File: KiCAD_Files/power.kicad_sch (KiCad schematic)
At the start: 100 parts, among them J1 Conn_01x01, J2 Conn_01x01, J3 Conn_01x01, J5 Conn_01x01, J8 Conn_01x01, K1 HF140FF/012-2HSWTF, Q11 NMOS, T1 Transformer_1P_1S, T2 Transformer_1P_1S, U1 INA240A1PW, U2 INA240A1PWR, U3 UCC27282DRC, U4 UCC27282DRC

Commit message: First routing pass complete.
Signed-off-by: Jean Alinei <jean.alinei@owntech.org>
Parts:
- removed C2, C4: C_Small, Capacitor_SMD:C_0805_2012Metric, symbol Device:C_Small
- removed C55: C, symbol Device:C
- added C101, C102: 4.7uF, Capacitor_SMD:C_0805_2012Metric, symbol Device:C_Small
- added C103, C110: 10µF, Capacitor_SMD:C_1206_3216Metric, symbol Device:C
- added C104, C105, C106, C107, C108, C109: C, Capacitor_SMD:C_1206_3216Metric, symbol Device:C
- added C111: 47uF, Capacitor_SMD:C_Elec_10x10.2, symbol Device:C_Polarized
- added C112: 47uH, Capacitor_SMD:C_Elec_10x10.2, symbol Device:C_Polarized
- added C113: ?nF, Capacitor_THT:C_Rect_L16.5mm_W7.0mm_P15.00mm_MKT, symbol Device:C_Small
- added C114, C115: 1nF, Capacitor_SMD:C_1210_3225Metric, symbol Device:C
- added D101, D102: D, Footprints:D_SOD-123, symbol Device:D
- added F101: 2.5A, Footprints:FUSE-TH_L8.4-W4.1-P5.08-D0.6, symbol Device:Fuse
- added HS101, HS102, HS103, HS104, HS105, HS106, HS107, HS108, HS109, HS11, HS12, HS5: 5x3mm pad 3mm high, Footprints:BTC-533-ZN01, symbol Mechanical:Heatsink_Pad
- added Logo101: ~, Footprints:owntech_mini10, symbol Symbols:Logo
- added R102, R103: 3.3R, Resistor_SMD:R_0805_2012Metric, symbol Device:R_Small
- added R104, R105, R106, R107, R108: 20, Resistor_SMD:R_0603_1608Metric, symbol Device:R_Small
- added R109: 20k, Resistor_SMD:R_0603_1608Metric, symbol Device:R_Small
- added RV101, RV102, RV103: TMOV14RP275, Varistor:RV_Disc_D12mm_W6.2mm_P7.5mm, symbol Device:Varistor
- C22, C27, C33, C38: footprint Capacitor_THT:C_Rect_L16.5mm_W8.7mm_P15.00mm_MKT -> Footprints:C_Rect_L16.5mm_W8mm_P15.00mm_MKT
- C39: footprint (none) -> Capacitor_SMD:C_0805_2012Metric
- D5: value D_Schottky -> 40V - BAT165E6327F; footprint Diode_SMD:D_SMA -> Diode_SMD:D_SOD-323; LCSC (none) -> C42411276
- F1: value T5A250V -> 2.5A; LCSC C42367993 -> C2995772
- FL1, FL2: symbol Device:Filter_EMI_CommonMode -> Device:L_Coupled_1243
- FL3: value ~ -> 1mH; footprint (none) -> Footprints:IND-TH_4P-L23.0-W15.0-P7.50-D1.0-S9.0; symbol Device:Filter_EMI_CommonMode -> Device:L_Coupled_1243
- Q1, Q2, Q3, Q4: value ~ -> CID12N65D
- Q10, Q5, Q6, Q7, Q8, Q9: value ~ -> CJAC90SN12
- Q11: value NMOS -> ZXMN7A11GTA; symbol Simulation_SPICE:NMOS -> Transistor_FET:Q_NMOS_GDSD; LCSC (none) -> C460277
- R101, R32, R33, R6, R8, R9: footprint Resistor_SMD:R_0805_2012Metric -> Resistor_SMD:R_0603_1608Metric
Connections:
- net Earth is gone; now on net Earth_Protective: J3.1 (Pin_1)
- net +12V_{HV}: now also D101.2 (A), D102.2 (A)
- net +12V_{SN1}: now also C101.1, R102.1
- net +12V_{SN2}: now also C102.1, R103.1
- net AC Current sense/In+: now also F101.1; no longer J2.1 (Pin_1)
- net AC Current sense/In-: now also FL2.3; no longer FL2.4
- net Earth_Protective: now also RV102.2, RV103.2
- net GND_{HV}: now also C114.2, C115.2, HS102.1, HS103.1
- net GND_{LV}: now also FL3.3, C103.1, C104.1, C105.1, C106.1, C107.1, C108.1, C109.1, C110.1, C111.2, C112.2; no longer FL3.4
- net HO1: now also R105.2; no longer Q5.2 (G), R6.2
- net HO2: now also R107.2; no longer Q8.2 (G), R9.2
- net HV_{BUS}: now also C114.1, C115.1, HS101.1, HS5.1; no longer Q1.2 (D), Q1.3 (D), Q2.2 (D), Q2.3 (D)
- net LO1: now also R104.2, R108.2; no longer Q6.2 (G), Q7.2 (G), R32.2, R8.2
- net LO2: now also R106.2, R109.2; no longer Q10.2 (G), Q9.2 (G), R101.2, R33.2
- net SN1: now also C101.2; no longer Q3.2 (D), Q3.3 (D)
- net SN2: now also C102.2; no longer Q4.2 (D), Q4.3 (D)
- net V_{IHigh1}: now also HS104.1
- net V_{IHigh2}: now also HS109.1
- net V_{ILow}: now also C103.2, C104.2, C105.2, C106.2, C107.2, C108.2, C109.2, C110.2, C111.1, C112.1
- net at D5.2 (A), K1.1: now also Q11.2 (D), Q11.4 (D); no longer Q11.1 (D)
- net at FL1.2, K1.4: now also C113.1, RV101.1, RV102.1
- net at C10.2, K1.5: now also FL2.4; no longer FL2.3
- net at K1.6: now also FL1.3, C113.2, RV101.2, RV103.1; no longer FL1.4
- net at C18.2, C19.2, C20.2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: now also T1.11 (AB), T1.12 (AB); no longer T1.2 (AB)
- net at C54.2, J8.1 (Pin_1): now also FL3.4; no longer FL3.3
- net at L3.2, R3.2: now also FL1.4; no longer FL1.3
- net at C22.2, C27.1: now also T1.5 (SA); no longer T1.3 (SA)
- net at C29.2, C30.2, C31.2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: now also T2.11 (AB), T2.12 (AB); no longer T2.2 (AB)
- net at R12.2, R13.1: now also Q11.1 (G); no longer Q11.2 (G)
- net Rect1: now reaches D1.2 (A), D2.1 (K)
- net Rect1: now also T1.2 (SB), HS11.1; no longer T1.4 (SB)
- net at C33.2, C38.1: now also T2.5 (SA); no longer T2.3 (SA)
- net Rect2: now reaches D3.2 (A), D4.1 (K)
- net Rect2: now also T2.2 (SB), HS12.1; no longer T2.4 (SB)
- net HS1 renamed LSW1
- net LSW1: now also T1.8 (AA), T1.9 (AA), HS107.1, HS108.1; no longer T1.1 (AA)
- net HS2 renamed LSW2
- net LSW2: now also T2.8 (AA), T2.9 (AA), HS105.1, HS106.1; no longer T2.1 (AA)
- new net: Q6.2 (G), R104.1, R32.2
- new net: Q7.2 (G), R108.1, R8.2
- new net: D102.1 (K), R103.2
- new net: D101.1 (K), R102.2
- new net: Q9.2 (G), R106.1, R33.2
- new net: Q8.2 (G), R107.1, R9.2
- new net: F101.2, J2.1 (Pin_1)
- new net: Q10.2 (G), R101.2, R109.1
- new net: Q5.2 (G), R105.1, R6.2
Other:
- note added: "0.6mA@12V"
- note added: "2.5mA@5V"
- note added: "67mA@12V"
- note added: "Low gate threshold to be driven directly by MCU"
- moved on the sheet: C10, C16, C17, C5, C6, D5, K1, Q6, Q9, R101, R12, R13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

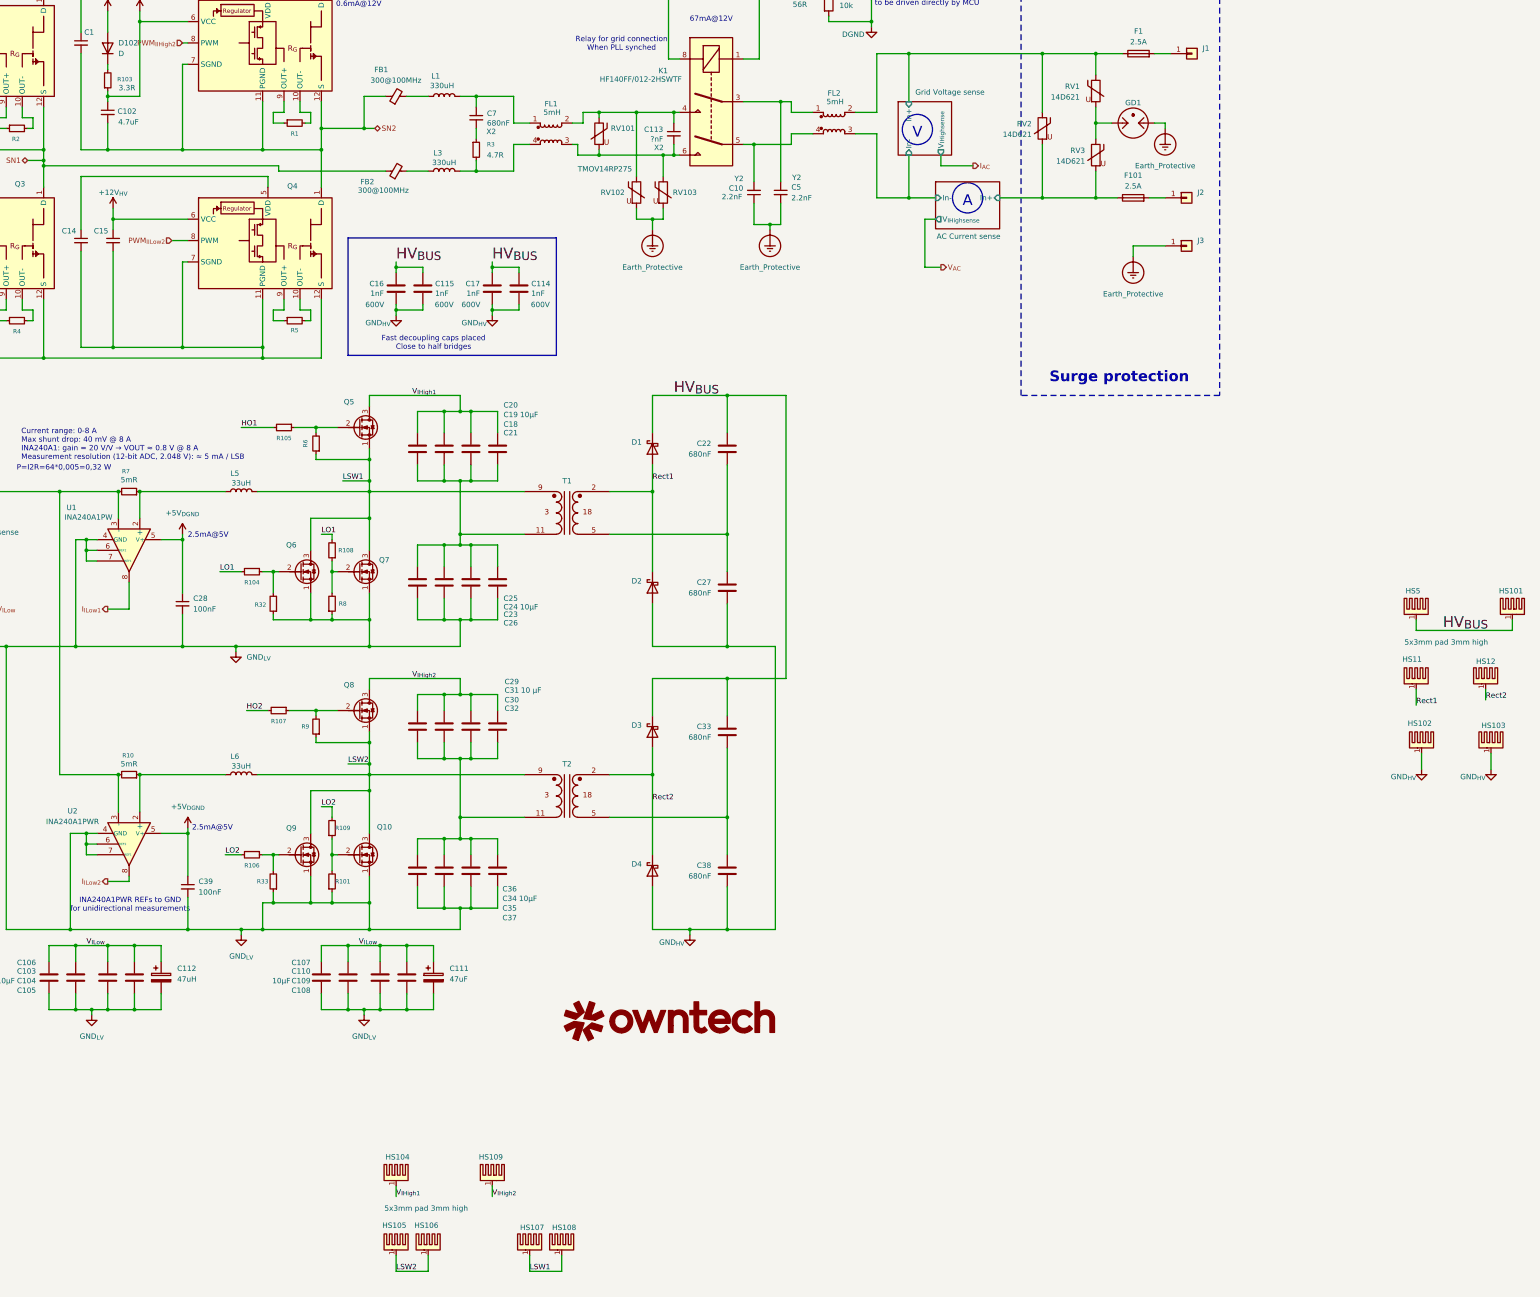
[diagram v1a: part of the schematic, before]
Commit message: Added missing tracks for sensors and relay. Fixed many routing issues.
Signed-off-by: Jean Alinei <jean.alinei@owntech.org>
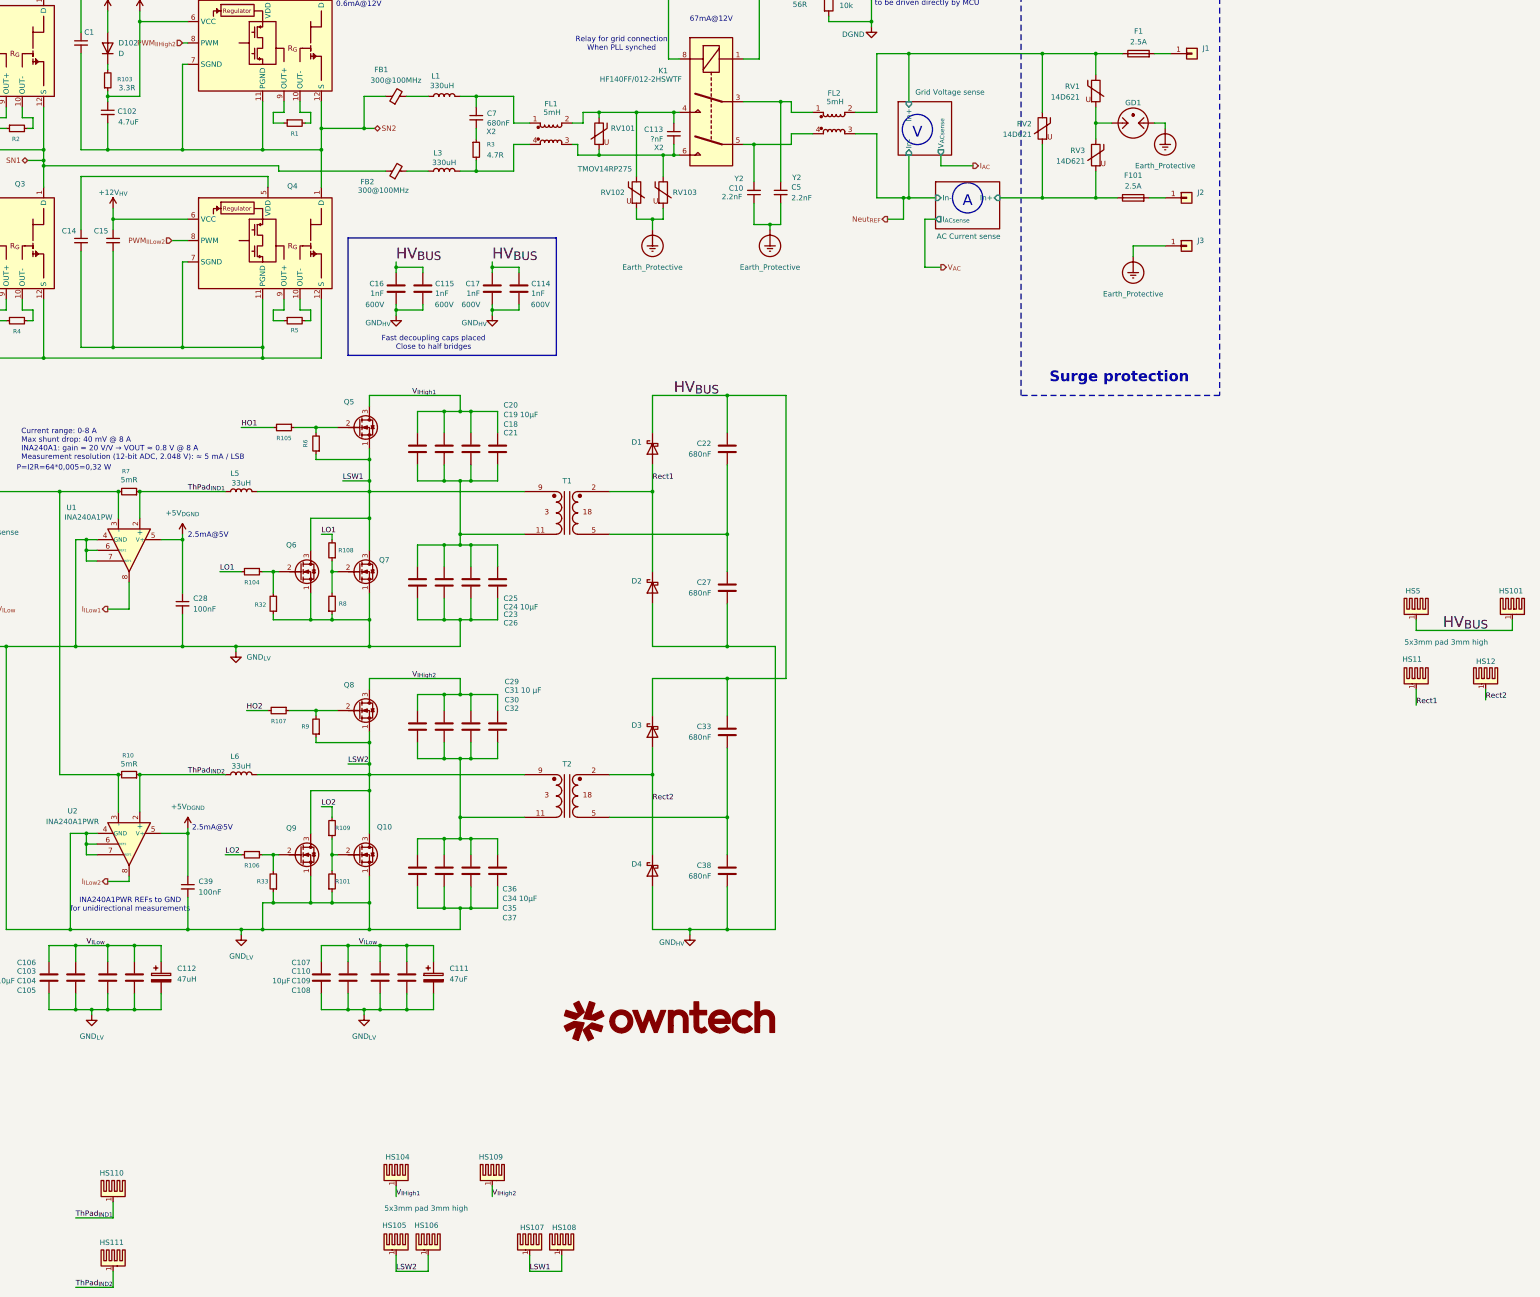
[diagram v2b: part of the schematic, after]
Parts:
- removed HS102, HS103: 5x3mm pad 3mm high, Footprints:BTC-533-ZN01, symbol Mechanical:Heatsink_Pad
- added HS110, HS111: 5x3mm pad 3mm high, Footprints:BTC-533-ZN01, symbol Mechanical:Heatsink_Pad
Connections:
- net ThPad_{IND2}: now reaches L6.1, R10.1, U2.2 (+)
- net ThPad_{IND2}: now also HS111.1
- net ThPad_{IND1}: now reaches L5.1, R7.1, U1.2 (+)
- net ThPad_{IND1}: now also HS110.1
- net AC Current sense/In- renamed Neut_{REF}
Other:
- sheet AC Current sense ports: added I_{ACsense}; removed V_{IHighsense}
- sheet Grid Voltage sense ports: added V_{ACsense}; removed V_{IHighsense}

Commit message: Added DRC rules according to IEC60664 and IPC2221.
Signed-off-by: Jean Alinei <jean.alinei@owntech.org>
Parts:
- added C116, C117: 2.2nF, Capacitor_THT:C_Rect_L9.0mm_W4.0mm_P7.50mm_MKT, symbol Device:C_Small
- added C118, C119: 1nF, Footprints:CAP-TH_L6.3-W4.4-P10.00-D0.6-S3.8, symbol Device:C_Small
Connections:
- net AC Current sense/In+: now also J2.1 (Pin_1); no longer F101.1
- net Earth_Protective: now also C116.1, C117.1
- net GND_{HV}: now also C118.2, C119.2
- net GND_{LV}: now also C117.2, C118.1, C119.1
- net Grid Voltage sense/In+: now also J1.1 (Pin_1); no longer F1.1
- net HV_{BUS}: now also Q1.4, Q2.4
- net SN1: now also Q3.4
- net SN2: now also Q4.4
- net V_{ILow}: now also C116.2
- net at C113.1, K1.4, RV102.1: now also F1.2; no longer FL1.2, RV101.1
- net at C113.2, K1.6, RV103.1: now also F101.2; no longer FL1.3, RV101.2
- net LSW4: now reaches C18.2, C19.2, C20.2, C21.2, C23.1, C24.1, C25.1, C26.1, T1.11 (AB), T1.12 (AB)
- net LSW3: now reaches C29.2, C30.2, C31.2, C32.2, C34.1, C35.1, C36.1, C37.1, T2.11 (AB), T2.12 (AB)
- new net: F1.1, FL1.2, RV101.1
- new net: F101.1, FL1.3, RV101.2
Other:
- sheet Input voltage sense ports: added V_{ILowsense}; removed V_{ILow}
- moved on the sheet: C10, C113, C5, D5, F1, F101, FL2, GD1, J1, J2, J3, K1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

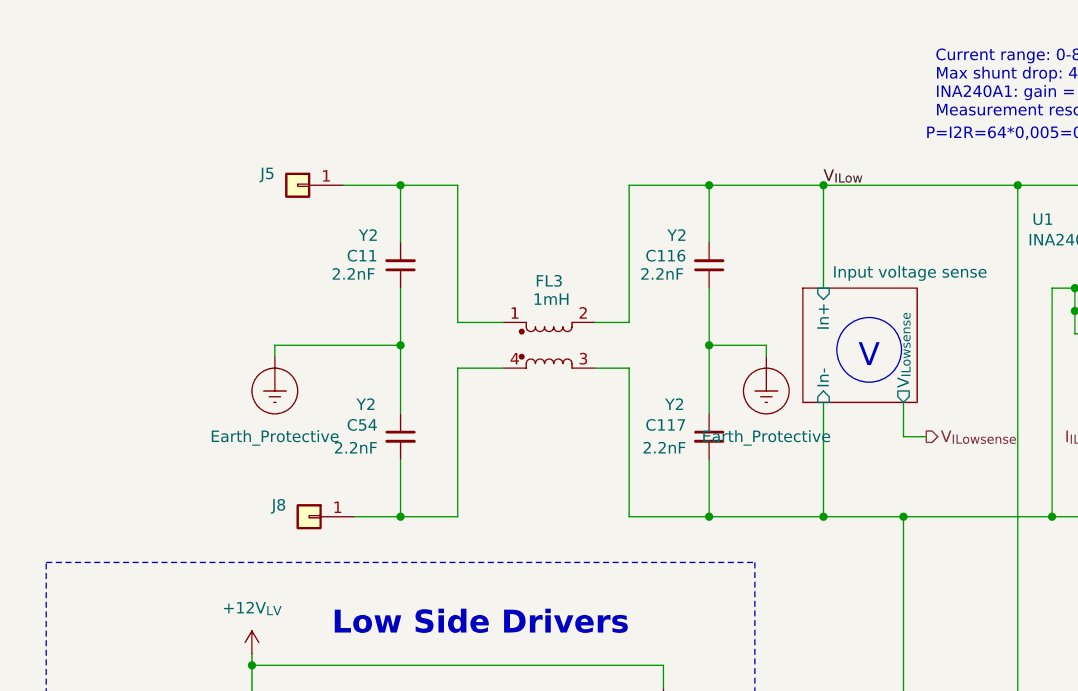
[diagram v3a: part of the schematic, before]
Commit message: Added PE keepouts. Adding thermal vias. DRC passing.
Signed-off-by: Jean Alinei <jean.alinei@owntech.org>
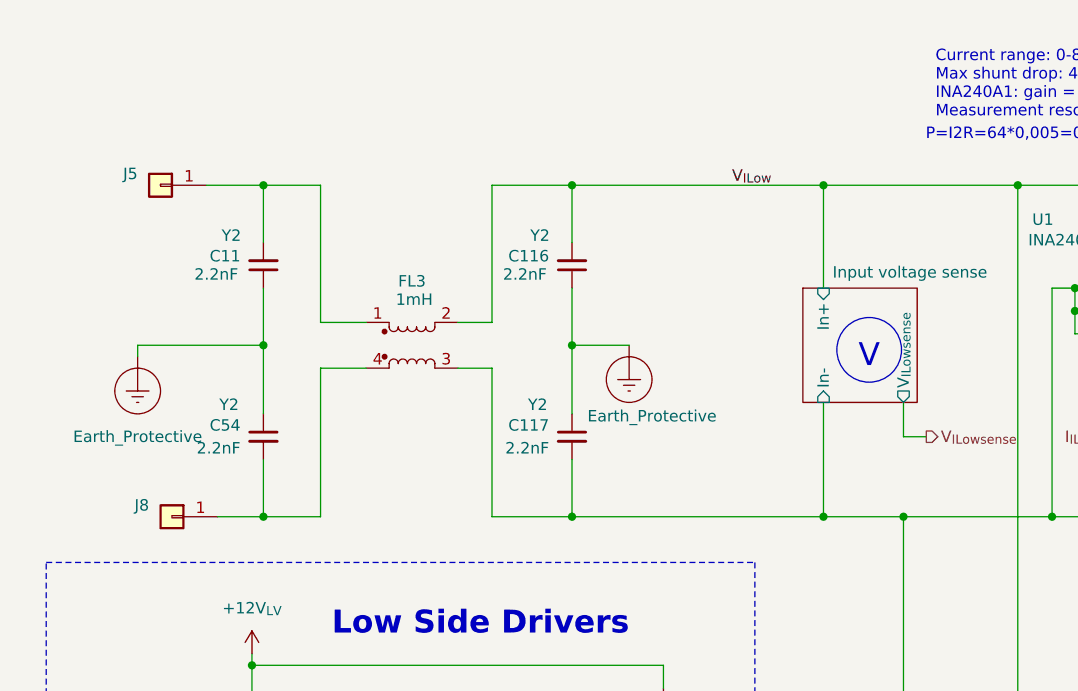
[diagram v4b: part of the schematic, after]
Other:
- moved on the sheet: C11, C116, C117, C54, FL3, J5, J8

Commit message: Added HF X2 caps, Improved low side Y2 placement. Improved Silkscreen.
Signed-off-by: Jean Alinei <jean.alinei@owntech.org>
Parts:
- added C120: 1nF, Capacitor_THT:C_Rect_L9.0mm_W4.0mm_P7.50mm_MKT, symbol Device:C_Small
- added C121: 680nF, Capacitor_THT:C_Rect_L16.5mm_W8.7mm_P15.00mm_MKT, symbol Device:C_Small
- Logo101: footprint Footprints:owntech_mini10 -> Footprints:owntech21mm
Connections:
- net GND_{HV}: now also C121.2
- net HV_{BUS}: now also C121.1
- net at C7.1, FL1.1, L1.2: now also C120.1
- net at FL1.4, L3.2, R3.2: now also C120.2
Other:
- moved on the sheet: C10, C113, C5, C6, C7, D5, F1, F101, FL1, FL2, GD1, J1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
